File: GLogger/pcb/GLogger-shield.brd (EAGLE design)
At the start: 68.6 x 53.3 mm, 10 parts, among them IC2 RV_3049_C2

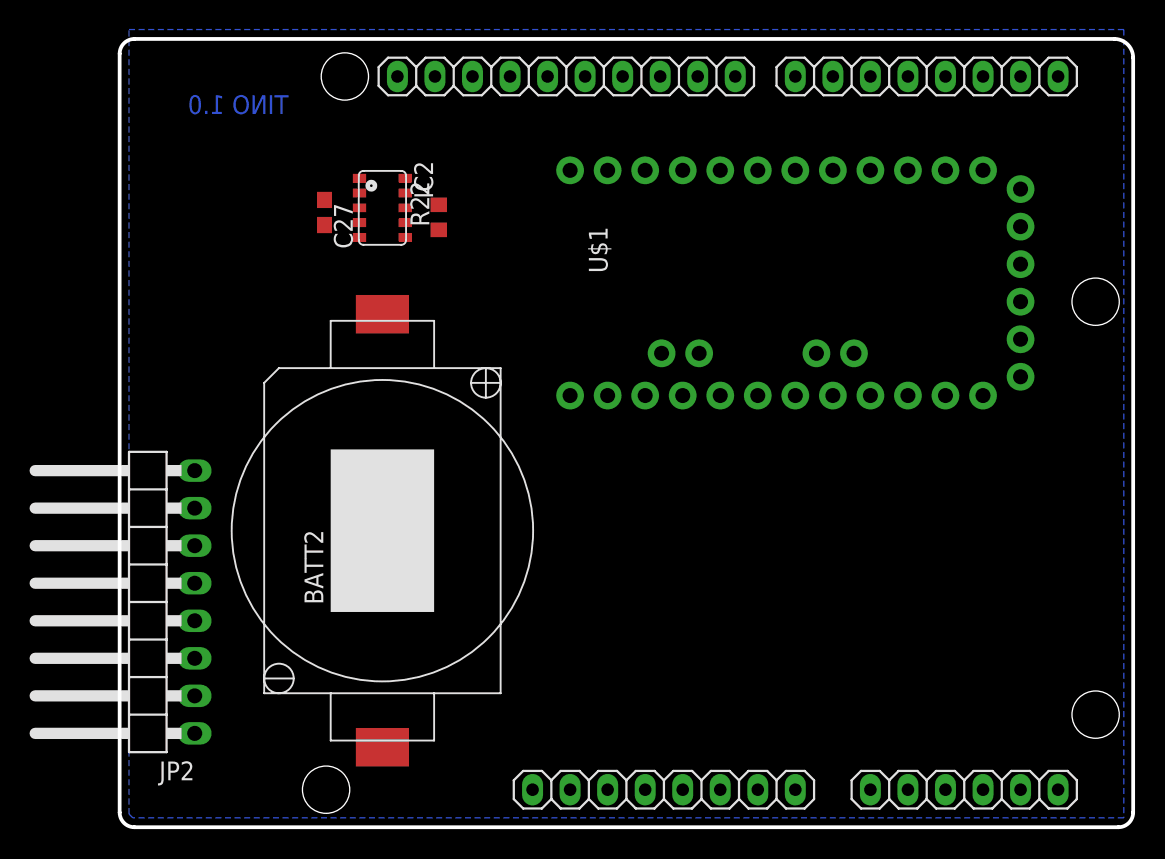
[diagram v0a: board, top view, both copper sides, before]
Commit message: ADXL345 and SC-Card.
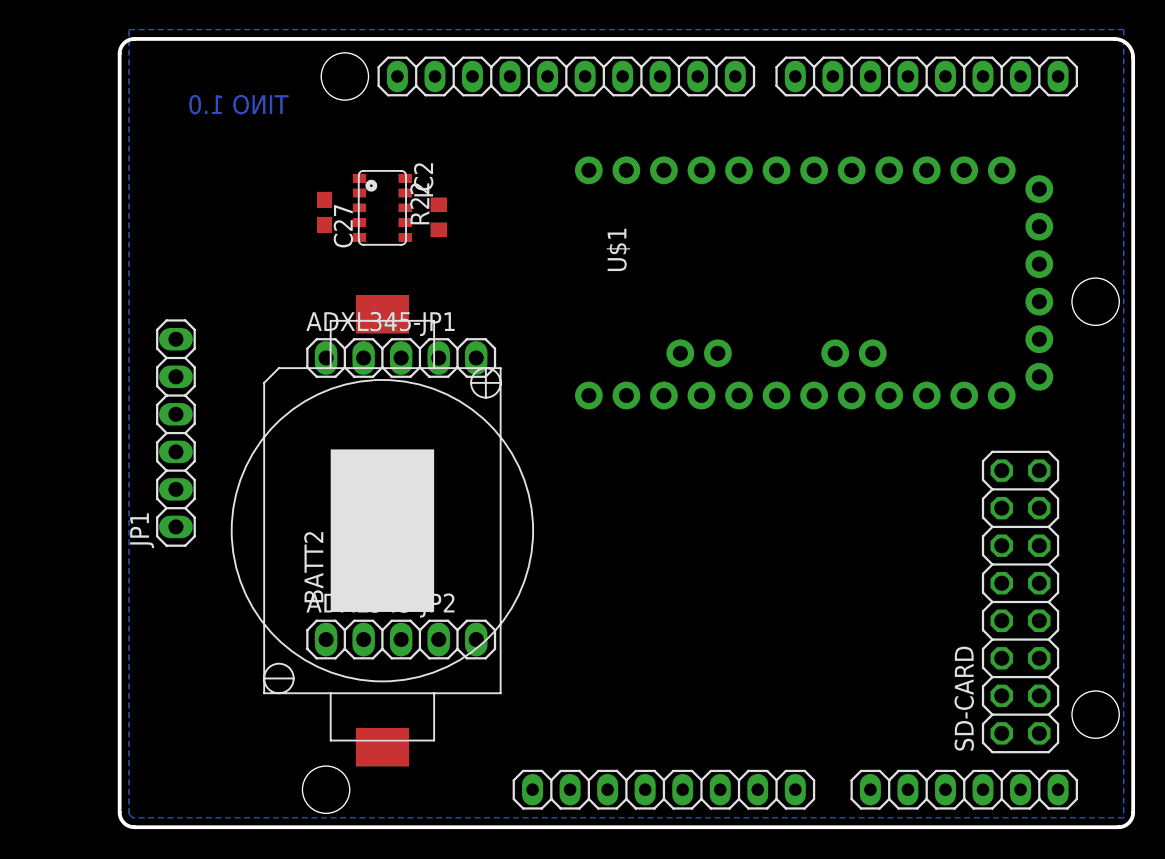
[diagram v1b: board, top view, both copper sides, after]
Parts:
- removed JP2: (no value), pinhead:1X08/90
- added ADXL345-JP1, ADXL345-JP2: (no value), pinhead:1X05
- added JP1: (no value), pinhead:1X06
- added SD-CARD: (no value), pinhead:2X08
- moved U$1 1.27 mm to (47.0, 36.8)
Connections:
- net +3V3: now also JP1.2; no longer JP2.2
- net +5V: now also ADXL345-JP1.1, JP1.1, SD-CARD.5; no longer JP2.1
- net A6: no longer JP2.7
- net A7: no longer JP2.8
- net AD4/SDA: now also ADXL345-JP2.1; no longer IC2.3
- net AD5/SCL: now also ADXL345-JP2.2
- net GND: now also ADXL345-JP1.2, JP1.3, SD-CARD.1; no longer JP2.3
- net IO0: now also JP1.5; no longer JP2.5
- net IO1: now also JP1.4; no longer JP2.4
- net IO9: now also IC2.3
- net MISO: now also SD-CARD.13
- net MOSI: now also SD-CARD.9
- net RESET: now also JP1.6; no longer JP2.6
- net SCK: now also SD-CARD.11
- net SS: now also SD-CARD.7

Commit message: switch to fat16.
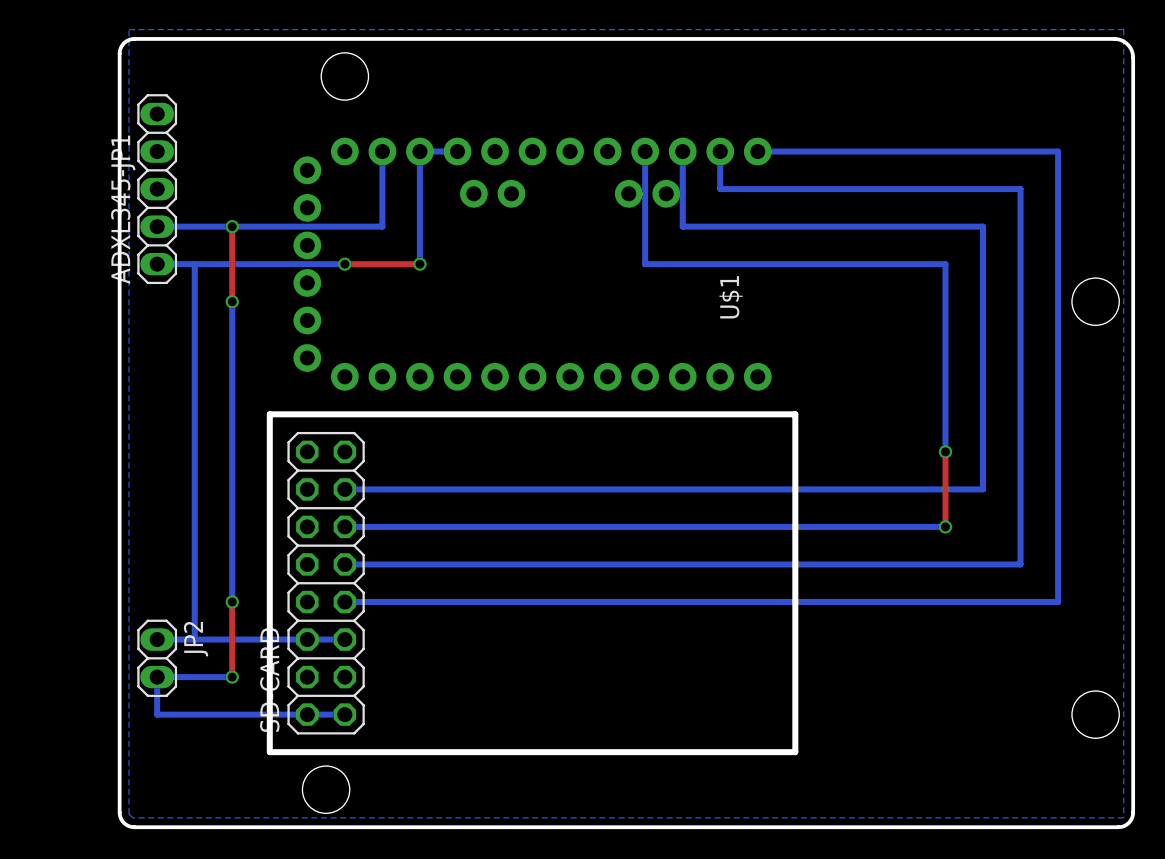
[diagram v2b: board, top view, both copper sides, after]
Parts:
- removed AD: 6x1F-H8.5, SmartPrj:1X06
- removed ADXL345-JP2: (no value), pinhead:1X05
- removed BATT2: 2032, El_Mech:2032_SMD
- removed C27: 100nF, rcl:C0603
- removed IC2: RV_3049_C2, RTC_Quarz:5X3.2_10
- removed IOH: 10x1F-H8.5, SmartPrj:1X10@1
- removed IOL, POWER: 8x1F-H8.5, SmartPrj:1X08
- removed JP1: (no value), pinhead:1X06
- removed R22: 330R, rcl:R0603
- added JP2: (no value), pinhead:1X02
- moved SD-CARD 47.0 mm to (14.0, 16.5)
- moved ADXL345-JP1 20.1 mm to (2.54, 43.2), turned to 90 degrees
- moved U$1 19.1 mm to (27.9, 38.1), turned to 90 degrees
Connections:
- removed net +3V3: JP1.2, POWER.4
- removed net +BAT: BATT2.+, R22.1
- removed net A6: U$1.A6
- removed net A7: U$1.A7
- removed net AD0: AD.1, U$1.17
- removed net AD1: AD.2, U$1.18
- removed net AD2: AD.3, U$1.19
- removed net AD3: AD.4, U$1.20
- removed net AD4/SDA': AD.5
- removed net AD5/SCL': AD.6
- removed net AREF: IOH.8
- removed net IO0: IOL.1, JP1.5, U$1.2
- removed net IO1: IOL.2, JP1.4, U$1.1
- removed net IO2: IOL.3, U$1.5
- removed net IO3: IOL.4, U$1.6
- removed net IO4: IOL.5, U$1.7
- removed net IO5: IOL.6, U$1.8
- removed net IO6: IOL.7, U$1.9
- removed net IO7: IOL.8, U$1.10
- removed net IO8: IOH.1, U$1.11
- removed net IO9: IC2.3, IOH.2, U$1.12
- removed net N$25: IC2.8, R22.2
- removed net RESET: JP1.6, POWER.3, U$1.3
- removed net VIN: POWER.8
- net +5V: now also JP2.1; no longer C27.1, IC2.1, JP1.1, POWER.2, POWER.5
- net AD4/SDA: now also ADXL345-JP1.3; no longer ADXL345-JP2.1, IOH.9
- net AD5/SCL: now also ADXL345-JP1.4; no longer ADXL345-JP2.2, IOH.10
- net GND: now also JP2.2; no longer BATT2.-, C27.2, IC2.6, IOH.7, JP1.3, POWER.6, POWER.7
- net MISO: no longer IC2.5, IOH.5
- net MOSI: no longer IC2.9, IOH.4
- net SCK: no longer IC2.4, IOH.6
- net SS: no longer IOH.3
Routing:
- net SS: track 0.00 -> 99.1 mm
- net MOSI: track 0.00 -> 94.0 mm
- net SCK: track 0.00 -> 86.4 mm, vias 0 -> 2
- net MISO: track 0.00 -> 86.4 mm
- net GND: track 0.00 -> 71.1 mm, vias 0 -> 4
- net +5V: track 0.00 -> 66.0 mm, vias 0 -> 2
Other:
- outline, holes or cut-outs redrawn
- board text removed: "TINO 1.0"

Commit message: new Layout.
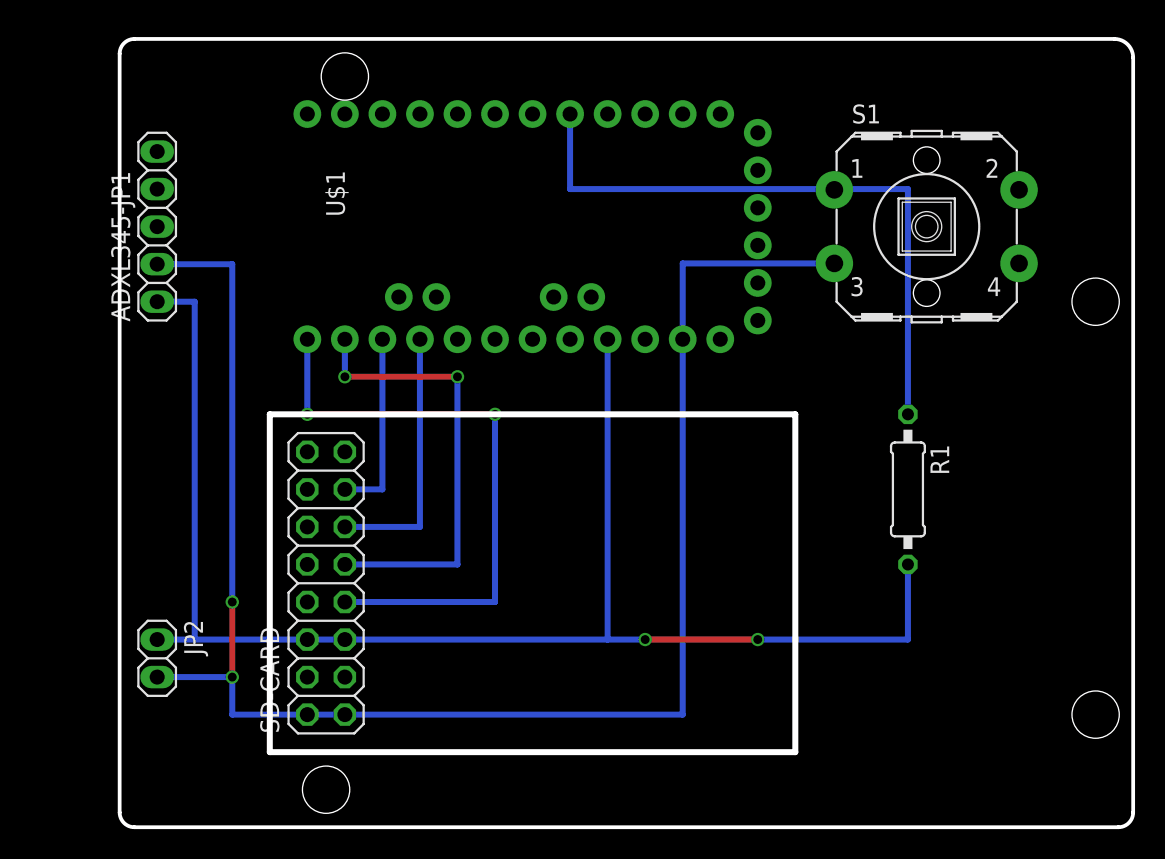
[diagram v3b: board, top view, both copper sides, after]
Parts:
- added R1: (no value), resistor:0207/10
- added S1: (no value), arduino_adafruit:B3F-40XX-ROUND
- moved ADXL345-JP1 2.54 mm to (2.54, 40.6)
- moved U$1 2.54 mm to (27.9, 40.6), turned to 270 degrees
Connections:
- new net IO2: R1.1, S1.1, U$1.5
- net +5V: now also R1.2
- net GND: now also S1.3
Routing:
- net MISO: track 86.4 -> 12.7 mm
- net SCK: track 86.4 -> 17.8 mm, vias 2 -> 0
- net MOSI: track 94.0 -> 30.5 mm, vias 0 -> 2
- net SS: track 99.1 -> 40.6 mm, vias 0 -> 2
- net IO2: track 0.00 -> 43.2 mm
- net GND: track 71.1 -> 111.9 mm, vias 4 -> 2
- net +5V: track 66.0 -> 101.6 mm
- removed copper zone on layer 16, net GND

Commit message: clean up.
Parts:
- removed ADXL345-JP1: (no value), pinhead:1X05
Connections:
- net +5V: no longer ADXL345-JP1.1
- net AD4/SDA: no longer ADXL345-JP1.3
- net AD5/SCL: no longer ADXL345-JP1.4
- net GND: no longer ADXL345-JP1.2
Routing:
- net GND: track 111.9 -> 78.9 mm, vias 2 -> 0
- net +5V: track 101.6 -> 76.2 mm
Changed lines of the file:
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@@
 <element name="U$1" library="SparkFun-Boards" package="ARDUINO_PRO_MINI" value="ARDUINO_PRO_MINI" x="27.94" y="40.64" rot="R270"/>
 <element name="SD-CARD" library="pinhead" package="2X08" value="" x="13.97" y="16.51" rot="R90"/>
-<element name="ADXL345-JP1" library="pinhead" package="1X05" value="" x="2.54" y="40.64" rot="R90"/>
 <element name="JP2" library="pinhead" package="1X02" value="" x="2.54" y="11.43" rot="R270"/>
 <element name="S1" library="arduino_adafruit" package="B3F-40XX-ROUND" value="" x="54.61" y="40.64"/>
@@
 <signal name="+5V" class="3">
 <contactref element="SD-CARD" pad="5"/>
-<contactref element="ADXL345-JP1" pad="1"/>
 <contactref element="U$1" pad="21"/>
 <contactref element="JP2" pad="1"/>
@@
 <via x="35.56" y="12.7" extent="1-16" drill="0.6" shape="square"/>
 <wire x1="35.56" y1="12.7" x2="33.02" y2="12.7" width="0.4064" layer="16"/>
-<wire x1="2.54" y1="12.7" x2="5.08" y2="12.7" width="0.4064" layer="16"/>
-<wire x1="5.08" y1="12.7" x2="15.24" y2="12.7" width="0.4064" layer="16"/>
-<wire x1="2.54" y1="35.56" x2="5.08" y2="35.56" width="0.4064" layer="16"/>
-<wire x1="5.08" y1="35.56" x2="5.08" y2="12.7" width="0.4064" layer="16"/>
+<wire x1="2.54" y1="12.7" x2="15.24" y2="12.7" width="0.4064" layer="16"/>
 </signal>
 <signal name="GND" class="2">
 <contactref element="U$1" pad="23"/>
 <contactref element="SD-CARD" pad="1"/>
-<contactref element="ADXL345-JP1" pad="2"/>
 <contactref element="JP2" pad="2"/>
 <contactref element="S1" pad="3"/>
@@
 <wire x1="38.1" y1="38.1508" x2="38.1" y2="33.02" width="0.4064" layer="16"/>
 <wire x1="2.54" y1="10.16" x2="7.62" y2="10.16" width="0.4064" layer="16"/>
+<wire x1="7.62" y1="10.16" x2="7.62" y2="7.62" width="0.4064" layer="16"/>
 <wire x1="7.62" y1="7.62" x2="15.24" y2="7.62" width="0.4064" layer="16"/>
-<wire x1="2.54" y1="38.1" x2="7.62" y2="38.1" width="0.4064" layer="16"/>
-<wire x1="7.62" y1="38.1" x2="7.62" y2="15.24" width="0.4064" layer="16"/>
-<via x="7.62" y="15.24" extent="1-16" drill="0.6" shape="square"/>
-<wire x1="7.62" y1="15.24" x2="7.62" y2="10.16" width="0.4064" layer="1"/>
-<via x="7.62" y="10.16" extent="1-16" drill="0.6" shape="square"/>
-<wire x1="7.62" y1="10.16" x2="7.62" y2="7.62" width="0.4064" layer="16"/>
 </signal>
 <signal name="SCK">
@@
 <signal name="AD4/SDA">
 <contactref element="U$1" pad="A4"/>
-<contactref element="ADXL345-JP1" pad="3"/>
-<wire x1="2.54" y1="40.64" x2="29.36875" y2="35.8775" width="0" layer="19" extent="1-1"/>
 </signal>
 <signal name="AD5/SCL">
 <contactref element="U$1" pad="A5"/>
-<contactref element="ADXL345-JP1" pad="4"/>
-<wire x1="2.54" y1="43.18" x2="31.90875" y2="35.8775" width="0" layer="19" extent="1-1"/>
 </signal>
 <signal name="IO2">
